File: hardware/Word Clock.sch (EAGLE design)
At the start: 27 parts, among them IC1 DS3231/SO, Q1 MMBT2222A, U1 ATMEGA328P-AU

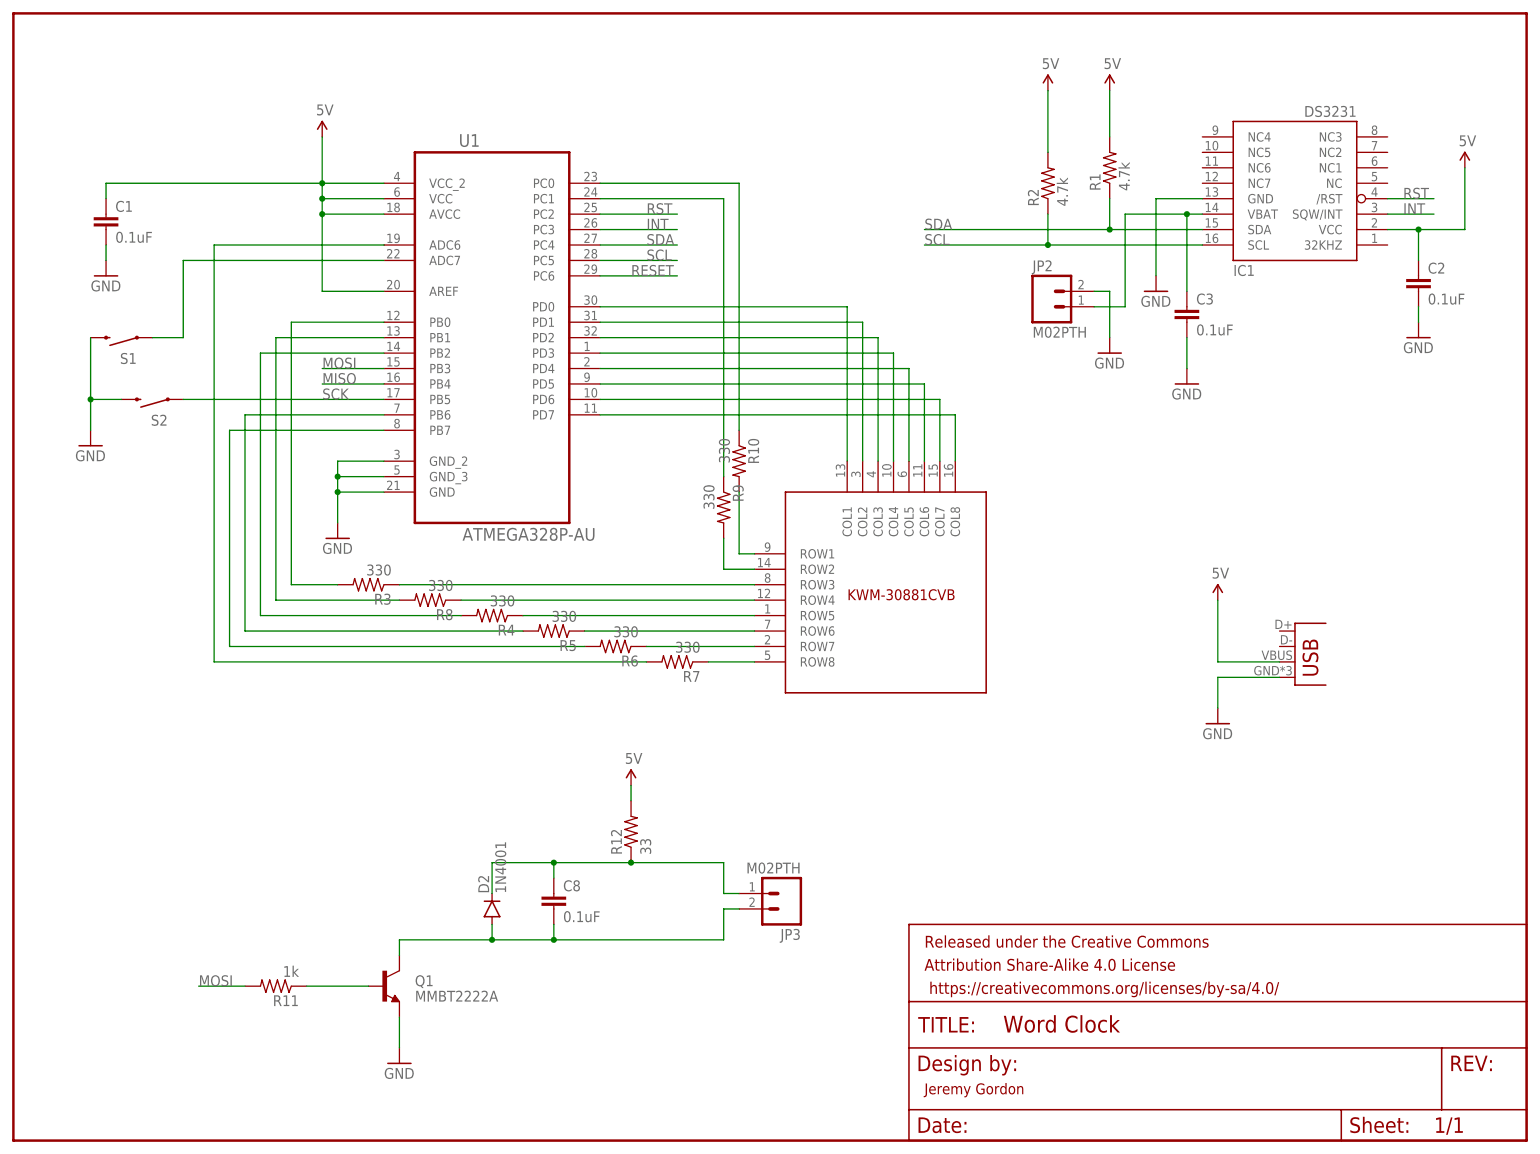
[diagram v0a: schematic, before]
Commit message: Fixing errant use of ADC lines and revised for 0.6mm vias.
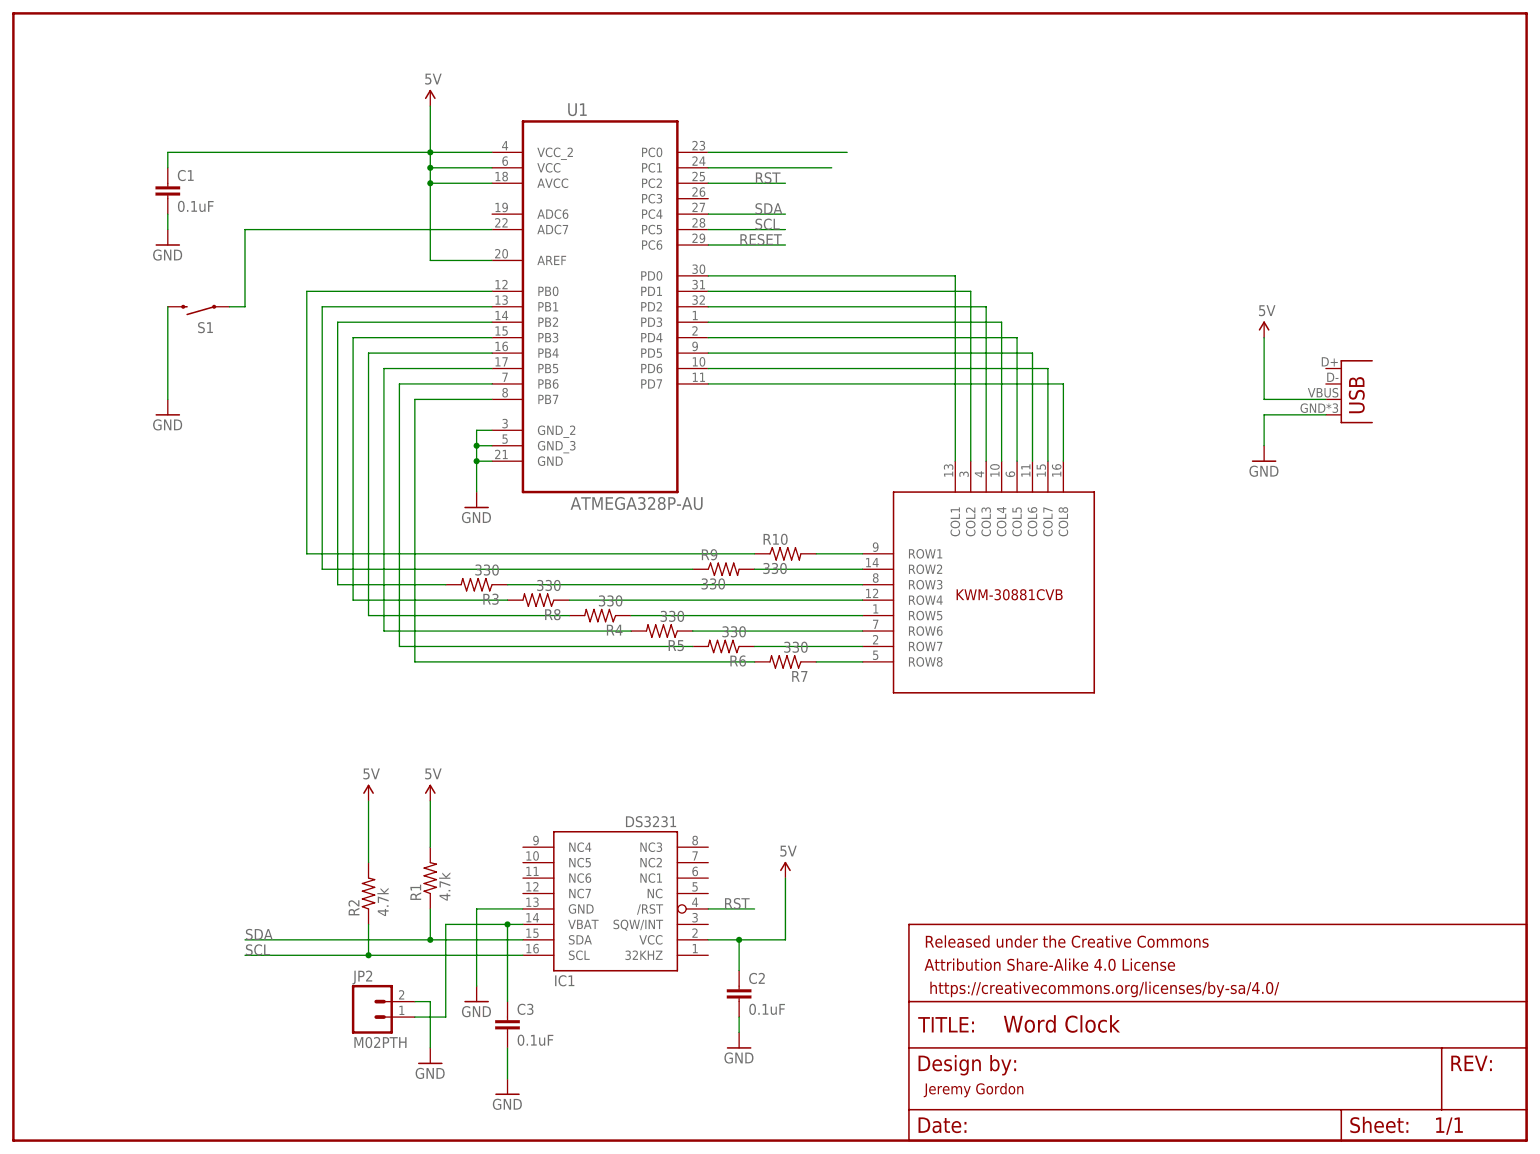
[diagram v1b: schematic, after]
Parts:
- removed C8: 0.1uF, SparkFun-Capacitors:CAP0805
- removed D2: 1N4001, SparkFun-DiscreteSemi:DIODESOD
- removed JP3: M02PTH, SparkFun-Connectors:M02PTH
- removed Q1: MMBT2222A, SparkFun-DiscreteSemi:TRANSISTOR_NPNMMBT2222A
- removed R11: 1k, SparkFun-Resistors:RESISTOR0805-RES
- removed R12: 33, SparkFun-Resistors:RESISTOR0805-RES
- removed S2: SWITCH-MOMENTARY-2SMD-1101NE, SparkFun-Electromechanical:SWITCH-MOMENTARY-2SMD-1101NE
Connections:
- removed net INT: IC1.SQW/INT, U1.PC3
- removed net MISO: U1.PB4
- removed net MOSI: R11.2, U1.PB3
- removed net N$16: R7.2, U1.ADC6
- removed net N$27: Q1.B, R11.1
- removed net N$28: C8.1, D2.C, JP3.1, R12.1
- removed net N$29: C8.2, D2.A, JP3.2, Q1.C
- removed net SCK: S2.1, U1.PB5
- new net N$30: R6.2, U1.PB6
- new net N$31: R7.2, U1.PB7
- new net N$33: R3.2, U1.PB2
- net 5V: no longer R12.2
- net GND: no longer Q1.E, S2.2
- net N$10: no longer R10.1
- net N$11: now also R9.1, U1.PB1; no longer R3.2, U1.PB0
- net N$12: now also U1.PB3; no longer U1.PB1
- net N$13: now also U1.PB4; no longer U1.PB2
- net N$14: now also U1.PB5; no longer U1.PB6
- net N$15: now also R10.1, U1.PB0; no longer R6.2, U1.PB7
- net N$9: no longer R9.1
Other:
- moved on the sheet: C1, C2, C3, IC1, JP2, R1, R10, R2, R3, R4, R5, R6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
